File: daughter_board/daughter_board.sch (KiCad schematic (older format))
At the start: 7 parts, among them J1 AudioJack4, SW1 SW_Push, SW2 Rotary_Encoder

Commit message: finished main board pcb
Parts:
- removed J1: AudioJack4, Connector_Audio:Jack_3.5mm_CUI_SJ-3523-SMT_Horizontal, symbol Connector:AudioJack4
- added J1: SJ2-3574A-SMT-TR, TRRS_jack:CUI_SJ2-3574A-SMT-TR, symbol SJ2-3574A-SMT-TR:SJ2-3574A-SMT-TR
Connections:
- net GND: now also J1.2
- net OUT_A: now also J1.4
- net OUT_B: now also J1.3
- net at SW1.1: now also J1.1
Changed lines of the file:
@@
 	1    0    0    -1
 $EndComp
-$Comp
-L Connector:AudioJack4 J1
-U 1 1 5F9D5189
-P 2850 1500
-F 0 "J1" H 2807 1825 50  0000 C CNN
-F 1 "AudioJack4" H 2807 1734 50  0000 C CNN
-F 2 "Connector_Audio:Jack_3.5mm_CUI_SJ-3523-SMT_Horizontal" H 2850 1500 50  0001 C CNN
-F 3 "~" H 2850 1500 50  0001 C CNN
-	1    2850 1500
-	1    0    0    -1
-$EndComp
-Wire Wire Line
-	3050 1700 3400 1700
 Text GLabel 3400 1700 2    50   Input ~ 0
 GND
@@
 Wire Wire Line
 	3050 1500 3350 1500
+$Comp
+L SJ2-3574A-SMT-TR:SJ2-3574A-SMT-TR J1
+U 1 1 5FAF7605
+P 2550 1600
+F 0 "J1" H 2637 1981 50  0000 C CNN
+F 1 "SJ2-3574A-SMT-TR" H 2637 1890 50  0000 C CNN
+F 2 "TRRS_jack:CUI_SJ2-3574A-SMT-TR" H 2550 1600 50  0001 L BNN
+F 3 "" H 2550 1600 50  0001 L BNN
+F 4 "Manufacturer Recommendations" H 2550 1600 50  0001 L BNN "STANDARD"
+F 5 "5.3 mm" H 2550 1600 50  0001 L BNN "MAXIMUM_PACKAGE_HEIGHT"
+F 6 "CUI" H 2550 1600 50  0001 L BNN "MANUFACTURER"
+F 7 "1.02" H 2550 1600 50  0001 L BNN "PARTREV"
+	1    2550 1600
+	1    0    0    -1
+$EndComp
+Wire Wire Line
+	3150 1700 3150 1800
+Wire Wire Line
+	3150 1800 3050 1800
+Wire Wire Line
+	3150 1700 3400 1700
 $EndSCHEMATC

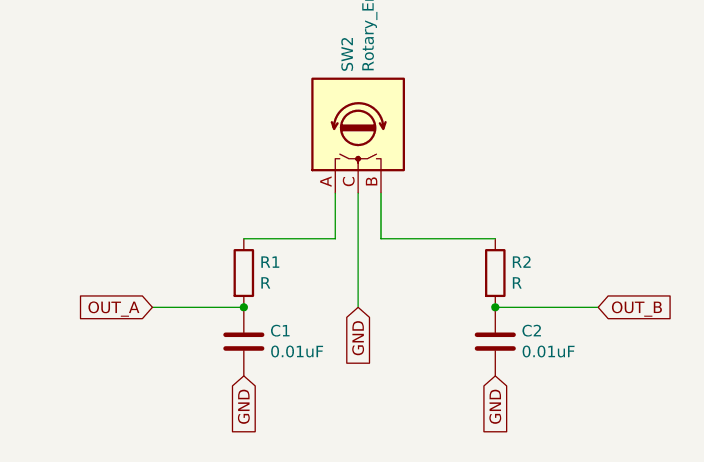
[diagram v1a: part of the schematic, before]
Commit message: modified connector location to avoid clerance issues
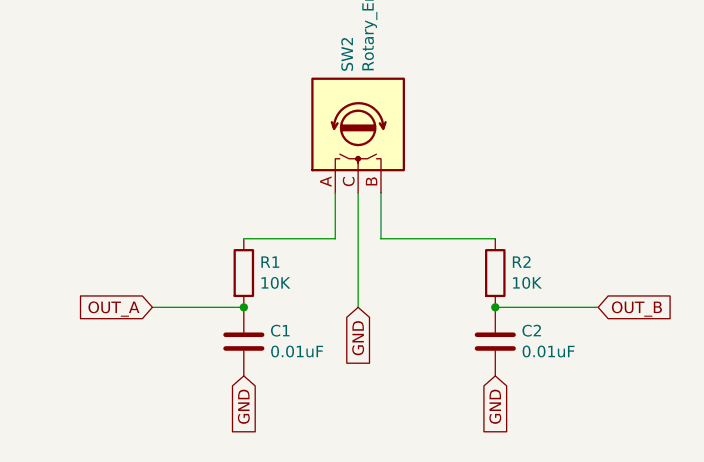
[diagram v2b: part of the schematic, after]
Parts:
- R1, R2: value R -> 10K
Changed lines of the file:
@@
 P 5750 2250
 F 0 "R1" H 5820 2296 50  0000 L CNN
-F 1 "R" H 5820 2205 50  0000 L CNN
+F 1 "10K" H 5820 2205 50  0000 L CNN
 F 2 "Resistor_SMD:R_1206_3216Metric_Pad1.30x1.75mm_HandSolder" V 5680 2250 50  0001 C CNN
 F 3 "~" H 5750 2250 50  0001 C CNN
@@
 P 6850 2250
 F 0 "R2" H 6920 2296 50  0000 L CNN
-F 1 "R" H 6920 2205 50  0000 L CNN
+F 1 "10K" H 6920 2205 50  0000 L CNN
 F 2 "Resistor_SMD:R_1206_3216Metric_Pad1.30x1.75mm_HandSolder" V 6780 2250 50  0001 C CNN
 F 3 "~" H 6850 2250 50  0001 C CNN

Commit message: updated trrs jack, old one was out of stock :(
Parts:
- J1: footprint TRRS_jack:CUI_SJ2-3574A-SMT-TR -> TRRS_jack:CUI_SJ2-35043A-SMT-TR
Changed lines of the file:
@@
 F 0 "J1" H 2637 1981 50  0000 C CNN
 F 1 "SJ2-3574A-SMT-TR" H 2637 1890 50  0000 C CNN
-F 2 "TRRS_jack:CUI_SJ2-3574A-SMT-TR" H 2550 1600 50  0001 L BNN
+F 2 "TRRS_jack:CUI_SJ2-35043A-SMT-TR" H 2550 1600 50  0001 L BNN
 F 3 "" H 2550 1600 50  0001 L BNN
 F 4 "Manufacturer Recommendations" H 2550 1600 50  0001 L BNN "STANDARD"

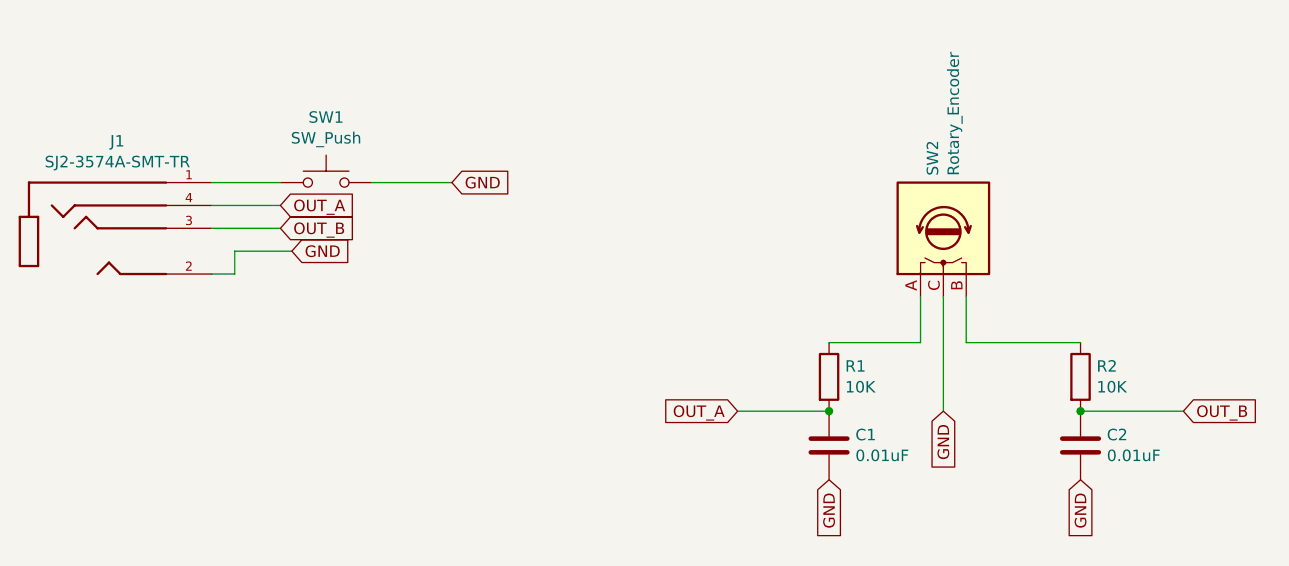
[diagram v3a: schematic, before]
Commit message: updated TRRS jack bc previous one was wrong one
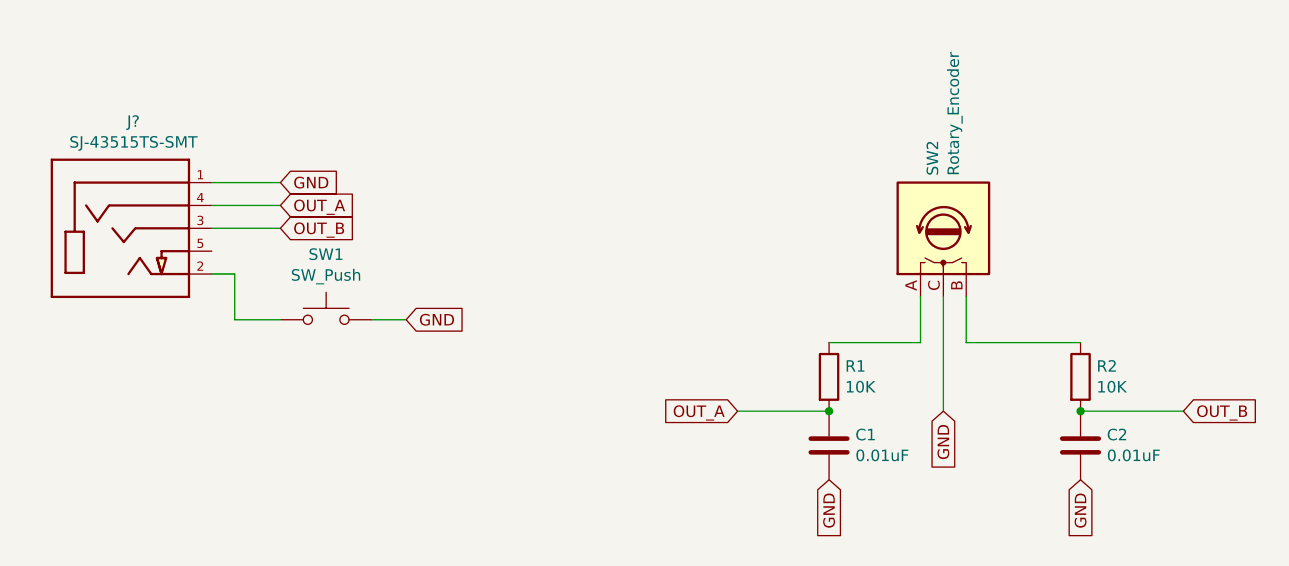
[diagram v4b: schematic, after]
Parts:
- removed J1: SJ2-3574A-SMT-TR, TRRS_jack:CUI_SJ2-35043A-SMT-TR, symbol SJ2-3574A-SMT-TR:SJ2-3574A-SMT-TR
- added J?: SJ-43515TS-SMT, CUI_SJ-43515TS-SMT, symbol SJ-43515TS-SMT:SJ-43515TS-SMT
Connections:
- net GND: now also J?.1
- net OUT_A: now also J?.4
- net OUT_B: now also J?.3
- net at SW1.1: now also J?.2
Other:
- moved on the sheet: SW1
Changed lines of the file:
@@
 L Switch:SW_Push SW1
 U 1 1 5F9D4304
-P 3550 1400
-F 0 "SW1" H 3550 1685 50  0000 C CNN
-F 1 "SW_Push" H 3550 1594 50  0000 C CNN
-F 2 "Button_Switch_Keyboard:SW_Cherry_MX_1.00u_PCB" H 3550 1600 50  0001 C CNN
-F 3 "~" H 3550 1600 50  0001 C CNN
-	1    3550 1400
+P 3550 2000
+F 0 "SW1" H 3550 2285 50  0000 C CNN
+F 1 "SW_Push" H 3550 2194 50  0000 C CNN
+F 2 "Button_Switch_Keyboard:SW_Cherry_MX_1.00u_PCB" H 3550 2200 50  0001 C CNN
+F 3 "~" H 3550 2200 50  0001 C CNN
+	1    3550 2000
 	1    0    0    -1
 $EndComp
-Text GLabel 3400 1700 2    50   Input ~ 0
+Text GLabel 3350 1400 2    50   Input ~ 0
 GND
 Wire Wire Line
 	3350 1400 3050 1400
-Wire Wire Line
-	3750 1400 4100 1400
-Text GLabel 4100 1400 2    50   Input ~ 0
+Text GLabel 3900 2000 2    50   Input ~ 0
 GND
 $Comp
@@
 Wire Wire Line
 	3050 1500 3350 1500
+Wire Wire Line
+	3150 1800 3050 1800
 $Comp
-L SJ2-3574A-SMT-TR:SJ2-3574A-SMT-TR J1
-U 1 1 5FAF7605
-P 2550 1600
-F 0 "J1" H 2637 1981 50  0000 C CNN
-F 1 "SJ2-3574A-SMT-TR" H 2637 1890 50  0000 C CNN
-F 2 "TRRS_jack:CUI_SJ2-35043A-SMT-TR" H 2550 1600 50  0001 L BNN
-F 3 "" H 2550 1600 50  0001 L BNN
-F 4 "Manufacturer Recommendations" H 2550 1600 50  0001 L BNN "STANDARD"
-F 5 "5.3 mm" H 2550 1600 50  0001 L BNN "MAXIMUM_PACKAGE_HEIGHT"
-F 6 "CUI" H 2550 1600 50  0001 L BNN "MANUFACTURER"
-F 7 "1.02" H 2550 1600 50  0001 L BNN "PARTREV"
-	1    2550 1600
+L SJ-43515TS-SMT:SJ-43515TS-SMT J?
+U 1 1 60585147
+P 2650 1600
+F 0 "J?" H 2707 2067 50  0000 C CNN
+F 1 "SJ-43515TS-SMT" H 2707 1976 50  0000 C CNN
+F 2 "CUI_SJ-43515TS-SMT" H 2650 1600 50  0001 L BNN
+F 3 "" H 2650 1600 50  0001 L BNN
+F 4 "CUI" H 2650 1600 50  0001 L BNN "MF"
+F 5 "4 conductor 3.5 mm Surface Mount Audio Jack w/ Tip Switch" H 2650 1600 50  0001 L BNN "DESCRIPTION"
+F 6 "SJ-43515TS-SMT" H 2650 1600 50  0001 L BNN "MP"
+F 7 "None" H 2650 1600 50  0001 L BNN "PACKAGE"
+F 8 "None" H 2650 1600 50  0001 L BNN "PRICE"
+F 9 "Unavailable" H 2650 1600 50  0001 L BNN "AVAILABILITY"
+	1    2650 1600
 	1    0    0    -1
 $EndComp
 Wire Wire Line
-	3150 1700 3150 1800
+	3350 2000 3150 2000
 Wire Wire Line
-	3150 1800 3050 1800
+	3150 2000 3150 1800
 Wire Wire Line
-	3150 1700 3400 1700
+	3900 2000 3750 2000
 $EndSCHEMATC
